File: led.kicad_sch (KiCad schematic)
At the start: 196 parts, among them U1 IS31FL3729, U2 IS31FL3729, U3 IS31FL3729, U4 IS31FL3729

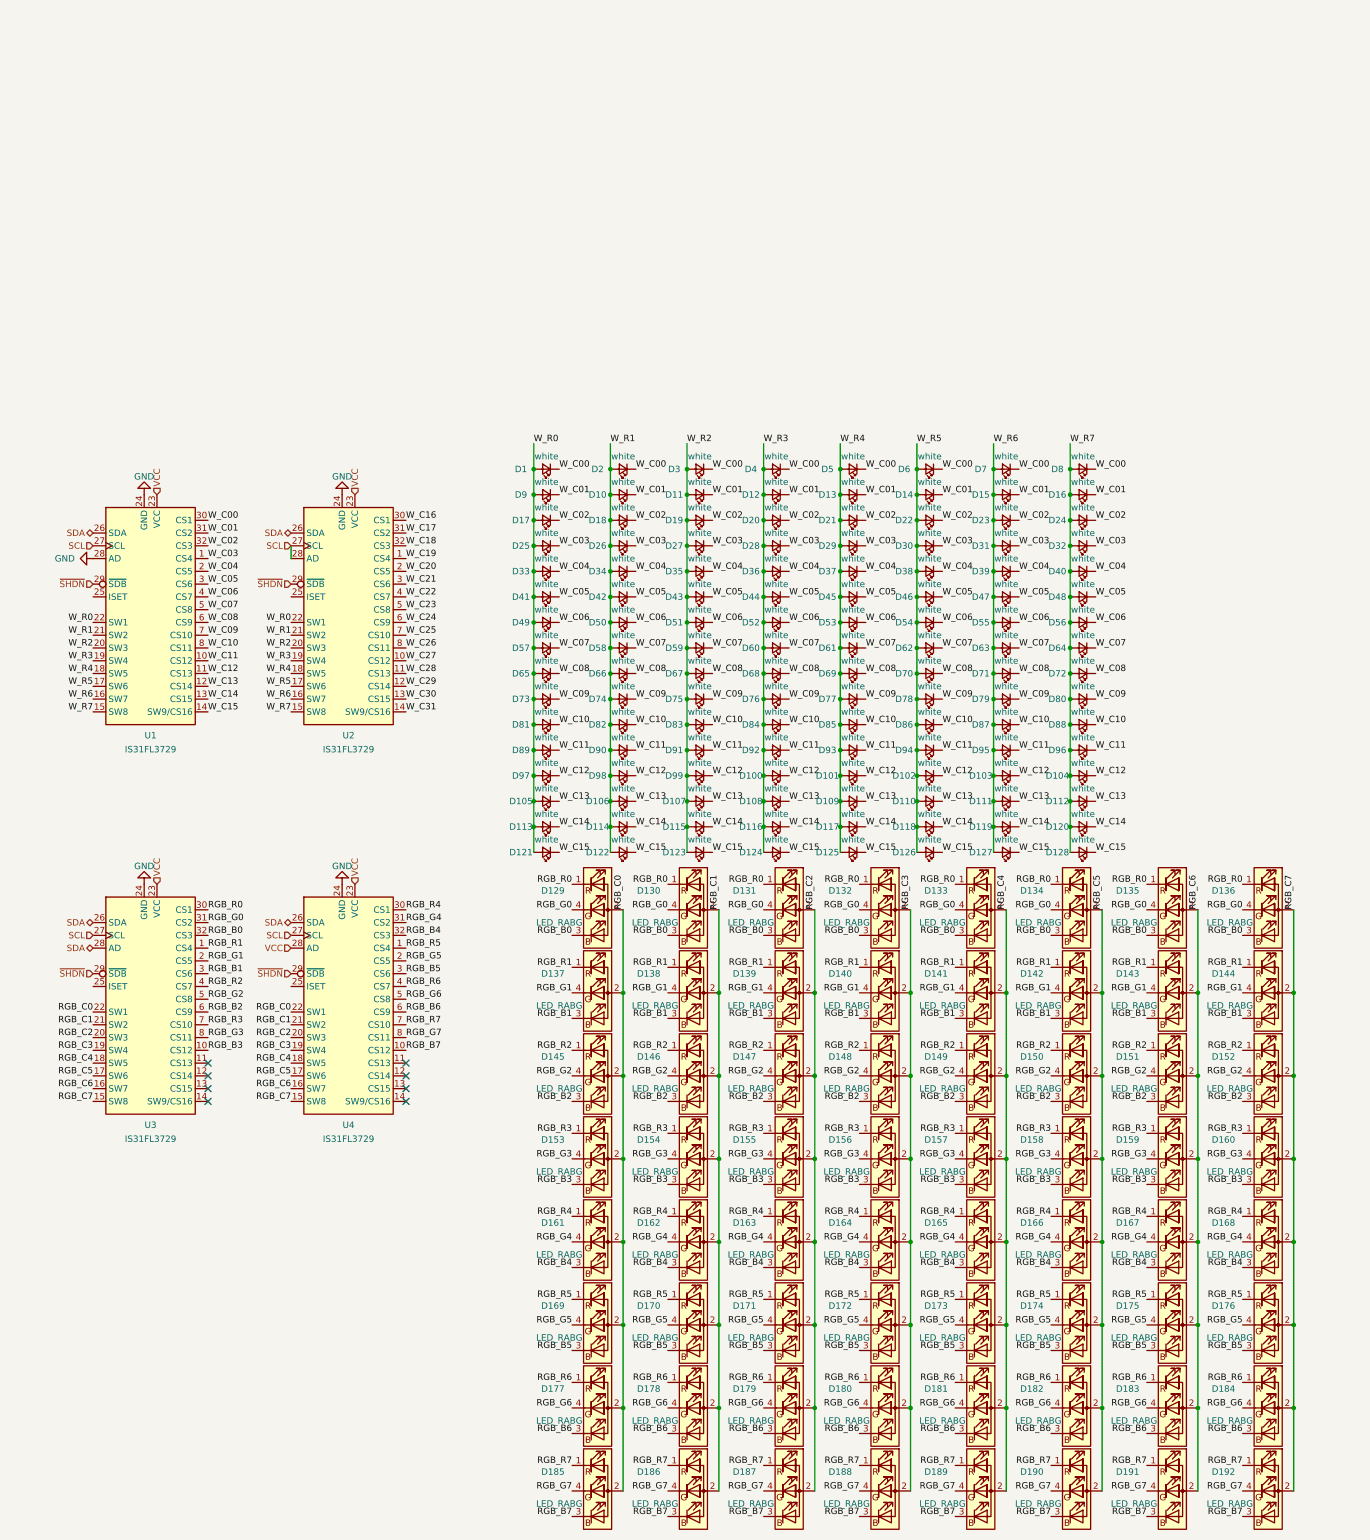
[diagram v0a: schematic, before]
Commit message: routed matrix + PWM driver
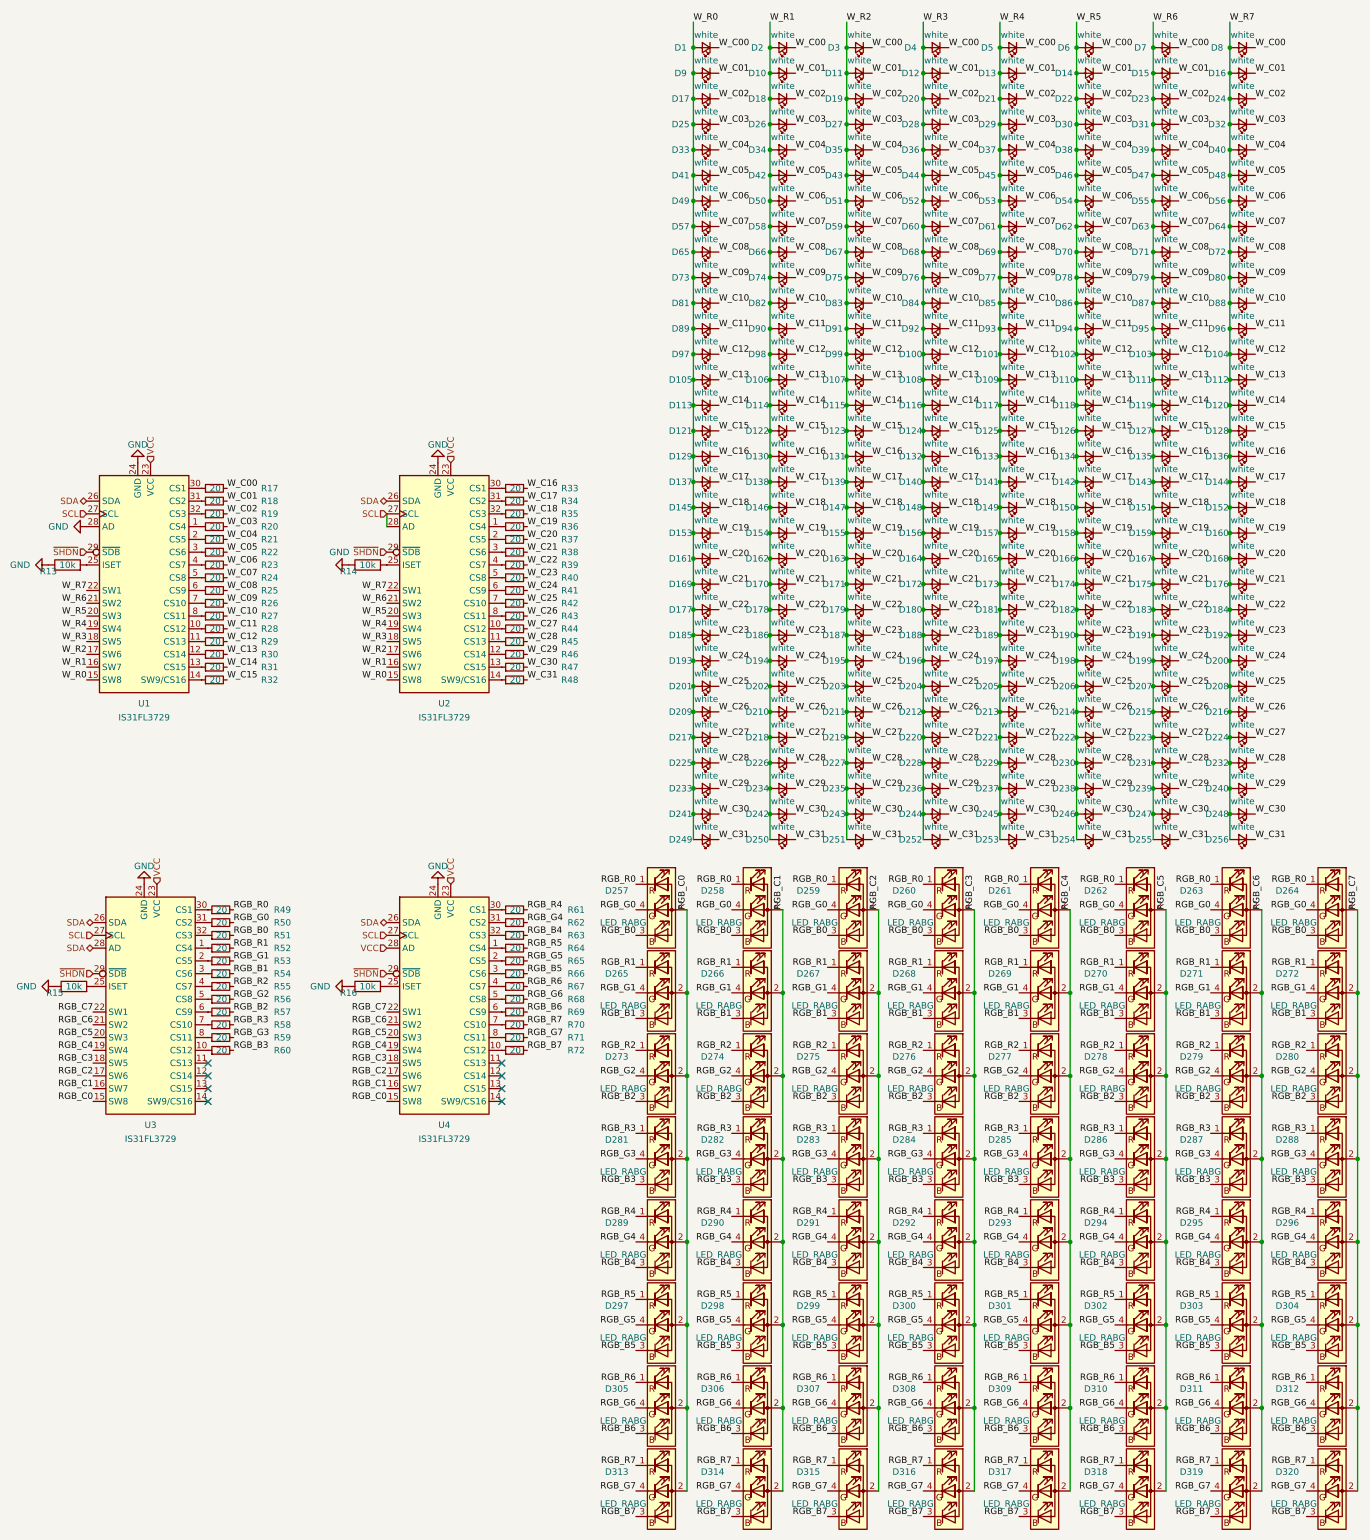
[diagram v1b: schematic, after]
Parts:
- added D129, D130, D131, D132, D133, D134, D135, D136, D137, D138, D139, D140, D141, D142, D143, D144, D145, D146, D147, D148, D149, D150, D151, D152, D153, D154, D155, D156, D157, D158, D159, D160, D161, D162, D163, D164, D165, D166, D167, D168, D169, D170, D171, D172, D173, D174, D175, D176, D177, D178, D179, D180, D181, D182, D183, D184, D185, D186, D187, D188, D189, D190, D191, D192, D193, D194, D195, D196, D197, D198, D199, D200, D201, D202, D203, D204, D205, D206, D207, D208, D209, D210, D211, D212, D213, D214, D215, D216, D217, D218, D219, D220, D221, D222, D223, D224, D225, D226, D227, D228, D229, D230, D231, D232, D233, D234, D235, D236, D237, D238, D239, D240, D241, D242, D243, D244, D245, D246, D247, D248, D249, D250, D251, D252, D253, D254, D255, D256: white, Diode_SMD:D_0603_1608Metric, symbol Device:LED_Small
- added R13, R14, R15, R16: 10k, Resistor_SMD:R_0603_1608Metric, symbol Device:R
- added R17, R18, R19, R20, R21, R22, R23, R24, R25, R26, R27, R28, R29, R30, R31, R32, R33, R34, R35, R36, R37, R38, R39, R40, R41, R42, R43, R44, R45, R46, R47, R48, R49, R50, R51, R52, R53, R54, R55, R56, R57, R58, R59, R60, R61, R62, R63, R64, R65, R66, R67, R68, R69, R70, R71, R72: 20, Resistor_SMD:R_0603_1608Metric, symbol Device:R_Small
- renumbered D129 to D257, D130 to D258, D131 to D259, D132 to D260, D133 to D261, D134 to D262, D135 to D263, D136 to D264, D137 to D265, D138 to D266, D139 to D267, D140 to D268, D141 to D269, D142 to D270, D143 to D271, D144 to D272, D145 to D273, D146 to D274, D147 to D275, D148 to D276, D149 to D277, D150 to D278, D151 to D279, D152 to D280, D153 to D281, D154 to D282, D155 to D283, D156 to D284, D157 to D285, D158 to D286, D159 to D287, D160 to D288, D161 to D289, D162 to D290, D163 to D291, D164 to D292, D165 to D293, D166 to D294, D167 to D295, D168 to D296, D169 to D297, D170 to D298, D171 to D299, D172 to D300, D173 to D301, D174 to D302, D175 to D303, D176 to D304, D177 to D305, D178 to D306, D179 to D307, D180 to D308, D181 to D309, D182 to D310, D183 to D311, D184 to D312, D185 to D313, D186 to D314, D187 to D315, D188 to D316, D189 to D317, D190 to D318, D191 to D319, D192 to D320
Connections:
- net GND: now also R13.1, R14.1, R15.1, R16.1
- net RGB_B0: now also R51.2; no longer U3.32 (CS3)
- net RGB_B1: now also R54.2; no longer U3.3 (CS6)
- net RGB_B2: now also R57.2; no longer U3.6 (CS9)
- net RGB_B3: now also R60.2; no longer U3.10 (CS12)
- net RGB_B4: now also R63.2; no longer U4.32 (CS3)
- net RGB_B5: now also R66.2; no longer U4.3 (CS6)
- net RGB_B6: now also R69.2; no longer U4.6 (CS9)
- net RGB_B7: now also R72.2; no longer U4.10 (CS12)
- net RGB_C0: now also U3.15 (SW8), U4.15 (SW8); no longer U3.22 (SW1), U4.22 (SW1)
- net RGB_C1: now also U3.16 (SW7), U4.16 (SW7); no longer U3.21 (SW2), U4.21 (SW2)
- net RGB_C2: now also U3.17 (SW6), U4.17 (SW6); no longer U3.20 (SW3), U4.20 (SW3)
- net RGB_C3: now also U3.18 (SW5), U4.18 (SW5); no longer U3.19 (SW4), U4.19 (SW4)
- net RGB_C4: now also U3.19 (SW4), U4.19 (SW4); no longer U3.18 (SW5), U4.18 (SW5)
- net RGB_C5: now also U3.20 (SW3), U4.20 (SW3); no longer U3.17 (SW6), U4.17 (SW6)
- net RGB_C6: now also U3.21 (SW2), U4.21 (SW2); no longer U3.16 (SW7), U4.16 (SW7)
- net RGB_C7: now also U3.22 (SW1), U4.22 (SW1); no longer U3.15 (SW8), U4.15 (SW8)
- net RGB_G0: now also R50.2; no longer U3.31 (CS2)
- net RGB_G1: now also R53.2; no longer U3.2 (CS5)
- net RGB_G2: now also R56.2; no longer U3.5 (CS8)
- net RGB_G3: now also R59.2; no longer U3.8 (CS11)
- net RGB_G4: now also R62.2; no longer U4.31 (CS2)
- net RGB_G5: now also R65.2; no longer U4.2 (CS5)
- net RGB_G6: now also R68.2; no longer U4.5 (CS8)
- net RGB_G7: now also R71.2; no longer U4.8 (CS11)
- net RGB_R0: now also R49.2; no longer U3.30 (CS1)
- net RGB_R1: now also R52.2; no longer U3.1 (CS4)
- net RGB_R2: now also R55.2; no longer U3.4 (CS7)
- net RGB_R3: now also R58.2; no longer U3.7 (CS10)
- net RGB_R4: now also R61.2; no longer U4.30 (CS1)
- net RGB_R5: now also R64.2; no longer U4.1 (CS4)
- net RGB_R6: now also R67.2; no longer U4.4 (CS7)
- net RGB_R7: now also R70.2; no longer U4.7 (CS10)
- net W_C00: now also R17.2; no longer U1.30 (CS1)
- net W_C01: now also R18.2; no longer U1.31 (CS2)
- net W_C02: now also R19.2; no longer U1.32 (CS3)
- net W_C03: now also R20.2; no longer U1.1 (CS4)
- net W_C04: now also R21.2; no longer U1.2 (CS5)
- net W_C05: now also R22.2; no longer U1.3 (CS6)
- net W_C06: now also R23.2; no longer U1.4 (CS7)
- net W_C07: now also R24.2; no longer U1.5 (CS8)
- net W_C08: now also R25.2; no longer U1.6 (CS9)
- net W_C09: now also R26.2; no longer U1.7 (CS10)
- net W_C10: now also R27.2; no longer U1.8 (CS11)
- net W_C11: now also R28.2; no longer U1.10 (CS12)
- net W_C12: now also R29.2; no longer U1.11 (CS13)
- net W_C13: now also R30.2; no longer U1.12 (CS14)
- net W_C14: now also R31.2; no longer U1.13 (CS15)
- net W_C15: now also R32.2; no longer U1.14 (SW9/CS16)
- net W_C16: now also D129.1 (K), D130.1 (K), D131.1 (K), D132.1 (K), D133.1 (K), D134.1 (K), D135.1 (K), D136.1 (K), R33.2; no longer U2.30 (CS1)
- net W_C17: now also D137.1 (K), D138.1 (K), D139.1 (K), D140.1 (K), D141.1 (K), D142.1 (K), D143.1 (K), D144.1 (K), R34.2; no longer U2.31 (CS2)
- net W_C18: now also D145.1 (K), D146.1 (K), D147.1 (K), D148.1 (K), D149.1 (K), D150.1 (K), D151.1 (K), D152.1 (K), R35.2; no longer U2.32 (CS3)
- net W_C19: now also D153.1 (K), D154.1 (K), D155.1 (K), D156.1 (K), D157.1 (K), D158.1 (K), D159.1 (K), D160.1 (K), R36.2; no longer U2.1 (CS4)
- net W_C20: now also D161.1 (K), D162.1 (K), D163.1 (K), D164.1 (K), D165.1 (K), D166.1 (K), D167.1 (K), D168.1 (K), R37.2; no longer U2.2 (CS5)
- net W_C21: now also D169.1 (K), D170.1 (K), D171.1 (K), D172.1 (K), D173.1 (K), D174.1 (K), D175.1 (K), D176.1 (K), R38.2; no longer U2.3 (CS6)
- net W_C22: now also D177.1 (K), D178.1 (K), D179.1 (K), D180.1 (K), D181.1 (K), D182.1 (K), D183.1 (K), D184.1 (K), R39.2; no longer U2.4 (CS7)
- net W_C23: now also D185.1 (K), D186.1 (K), D187.1 (K), D188.1 (K), D189.1 (K), D190.1 (K), D191.1 (K), D192.1 (K), R40.2; no longer U2.5 (CS8)
- net W_C24: now also D193.1 (K), D194.1 (K), D195.1 (K), D196.1 (K), D197.1 (K), D198.1 (K), D199.1 (K), D200.1 (K), R41.2; no longer U2.6 (CS9)
- net W_C25: now also D201.1 (K), D202.1 (K), D203.1 (K), D204.1 (K), D205.1 (K), D206.1 (K), D207.1 (K), D208.1 (K), R42.2; no longer U2.7 (CS10)
- net W_C26: now also D209.1 (K), D210.1 (K), D211.1 (K), D212.1 (K), D213.1 (K), D214.1 (K), D215.1 (K), D216.1 (K), R43.2; no longer U2.8 (CS11)
- net W_C27: now also D217.1 (K), D218.1 (K), D219.1 (K), D220.1 (K), D221.1 (K), D222.1 (K), D223.1 (K), D224.1 (K), R44.2; no longer U2.10 (CS12)
- net W_C28: now also D225.1 (K), D226.1 (K), D227.1 (K), D228.1 (K), D229.1 (K), D230.1 (K), D231.1 (K), D232.1 (K), R45.2; no longer U2.11 (CS13)
- net W_C29: now also D233.1 (K), D234.1 (K), D235.1 (K), D236.1 (K), D237.1 (K), D238.1 (K), D239.1 (K), D240.1 (K), R46.2; no longer U2.12 (CS14)
- net W_C30: now also D241.1 (K), D242.1 (K), D243.1 (K), D244.1 (K), D245.1 (K), D246.1 (K), D247.1 (K), D248.1 (K), R47.2; no longer U2.13 (CS15)
- net W_C31: now also D249.1 (K), D250.1 (K), D251.1 (K), D252.1 (K), D253.1 (K), D254.1 (K), D255.1 (K), D256.1 (K), R48.2; no longer U2.14 (SW9/CS16)
- net W_R0: now also U1.15 (SW8), U2.15 (SW8), D129.2 (A), D137.2 (A), D145.2 (A), D153.2 (A), D161.2 (A), D169.2 (A), D177.2 (A), D185.2 (A), D193.2 (A), D201.2 (A), D209.2 (A), D217.2 (A), D225.2 (A), D233.2 (A), D241.2 (A), D249.2 (A); no longer U1.22 (SW1), U2.22 (SW1)
- net W_R1: now also U1.16 (SW7), U2.16 (SW7), D130.2 (A), D138.2 (A), D146.2 (A), D154.2 (A), D162.2 (A), D170.2 (A), D178.2 (A), D186.2 (A), D194.2 (A), D202.2 (A), D210.2 (A), D218.2 (A), D226.2 (A), D234.2 (A), D242.2 (A), D250.2 (A); no longer U1.21 (SW2), U2.21 (SW2)
- net W_R2: now also U1.17 (SW6), U2.17 (SW6), D131.2 (A), D139.2 (A), D147.2 (A), D155.2 (A), D163.2 (A), D171.2 (A), D179.2 (A), D187.2 (A), D195.2 (A), D203.2 (A), D211.2 (A), D219.2 (A), D227.2 (A), D235.2 (A), D243.2 (A), D251.2 (A); no longer U1.20 (SW3), U2.20 (SW3)
- net W_R3: now also U1.18 (SW5), U2.18 (SW5), D132.2 (A), D140.2 (A), D148.2 (A), D156.2 (A), D164.2 (A), D172.2 (A), D180.2 (A), D188.2 (A), D196.2 (A), D204.2 (A), D212.2 (A), D220.2 (A), D228.2 (A), D236.2 (A), D244.2 (A), D252.2 (A); no longer U1.19 (SW4), U2.19 (SW4)
- net W_R4: now also U1.19 (SW4), U2.19 (SW4), D133.2 (A), D141.2 (A), D149.2 (A), D157.2 (A), D165.2 (A), D173.2 (A), D181.2 (A), D189.2 (A), D197.2 (A), D205.2 (A), D213.2 (A), D221.2 (A), D229.2 (A), D237.2 (A), D245.2 (A), D253.2 (A); no longer U1.18 (SW5), U2.18 (SW5)
- net W_R5: now also U1.20 (SW3), U2.20 (SW3), D134.2 (A), D142.2 (A), D150.2 (A), D158.2 (A), D166.2 (A), D174.2 (A), D182.2 (A), D190.2 (A), D198.2 (A), D206.2 (A), D214.2 (A), D222.2 (A), D230.2 (A), D238.2 (A), D246.2 (A), D254.2 (A); no longer U1.17 (SW6), U2.17 (SW6)
- net W_R6: now also U1.21 (SW2), U2.21 (SW2), D135.2 (A), D143.2 (A), D151.2 (A), D159.2 (A), D167.2 (A), D175.2 (A), D183.2 (A), D191.2 (A), D199.2 (A), D207.2 (A), D215.2 (A), D223.2 (A), D231.2 (A), D239.2 (A), D247.2 (A), D255.2 (A); no longer U1.16 (SW7), U2.16 (SW7)
- net W_R7: now also U1.22 (SW1), U2.22 (SW1), D136.2 (A), D144.2 (A), D152.2 (A), D160.2 (A), D168.2 (A), D176.2 (A), D184.2 (A), D192.2 (A), D200.2 (A), D208.2 (A), D216.2 (A), D224.2 (A), D232.2 (A), D240.2 (A), D248.2 (A), D256.2 (A); no longer U1.15 (SW8), U2.15 (SW8)
- net at U1.25 (ISET): now also R13.2
- net at U4.25 (ISET): now also R16.2
- net at U2.25 (ISET): now also R14.2
- net at U3.25 (ISET): now also R15.2
- new net: R20.1, U1.1 (CS4)
- new net: R28.1, U1.10 (CS12)
- new net: R29.1, U1.11 (CS13)
- new net: R30.1, U1.12 (CS14)
- new net: R31.1, U1.13 (CS15)
- new net: R32.1, U1.14 (SW9/CS16)
- new net: R21.1, U1.2 (CS5)
- new net: R22.1, U1.3 (CS6)
- new net: R17.1, U1.30 (CS1)
- new net: R18.1, U1.31 (CS2)
- new net: R19.1, U1.32 (CS3)
- new net: R23.1, U1.4 (CS7)
- new net: R24.1, U1.5 (CS8)
- new net: R25.1, U1.6 (CS9)
- new net: R26.1, U1.7 (CS10)
- new net: R27.1, U1.8 (CS11)
- new net: R47.1, U2.13 (CS15)
- new net: R72.1, U4.10 (CS12)
- new net: R59.1, U3.8 (CS11)
- new net: R42.1, U2.7 (CS10)
- new net: R40.1, U2.5 (CS8)
- new net: R34.1, U2.31 (CS2)
- new net: R39.1, U2.4 (CS7)
- new net: R52.1, U3.1 (CS4)
- new net: R38.1, U2.3 (CS6)
- new net: R60.1, U3.10 (CS12)
- new net: R36.1, U2.1 (CS4)
- new net: R67.1, U4.4 (CS7)
- new net: R64.1, U4.1 (CS4)
- new net: R65.1, U4.2 (CS5)
- new net: R66.1, U4.3 (CS6)
- new net: R61.1, U4.30 (CS1)
- new net: R62.1, U4.31 (CS2)
- new net: R63.1, U4.32 (CS3)
- new net: R68.1, U4.5 (CS8)
- new net: R69.1, U4.6 (CS9)
- new net: R70.1, U4.7 (CS10)
- new net: R71.1, U4.8 (CS11)
- new net: R33.1, U2.30 (CS1)
- new net: R44.1, U2.10 (CS12)
- new net: R45.1, U2.11 (CS13)
- new net: R46.1, U2.12 (CS14)
- new net: R48.1, U2.14 (SW9/CS16)
- new net: R37.1, U2.2 (CS5)
- new net: R35.1, U2.32 (CS3)
- new net: R41.1, U2.6 (CS9)
- new net: R43.1, U2.8 (CS11)
- new net: R54.1, U3.3 (CS6)
- new net: R49.1, U3.30 (CS1)
- new net: R58.1, U3.7 (CS10)
- new net: R51.1, U3.32 (CS3)
- new net: R50.1, U3.31 (CS2)
- new net: R55.1, U3.4 (CS7)
- new net: R57.1, U3.6 (CS9)
- new net: R56.1, U3.5 (CS8)
- new net: R53.1, U3.2 (CS5)
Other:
- moved on the sheet: D1, D10, D100, D101, D102, D103, D104, D105, D106, D107, D108, D109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

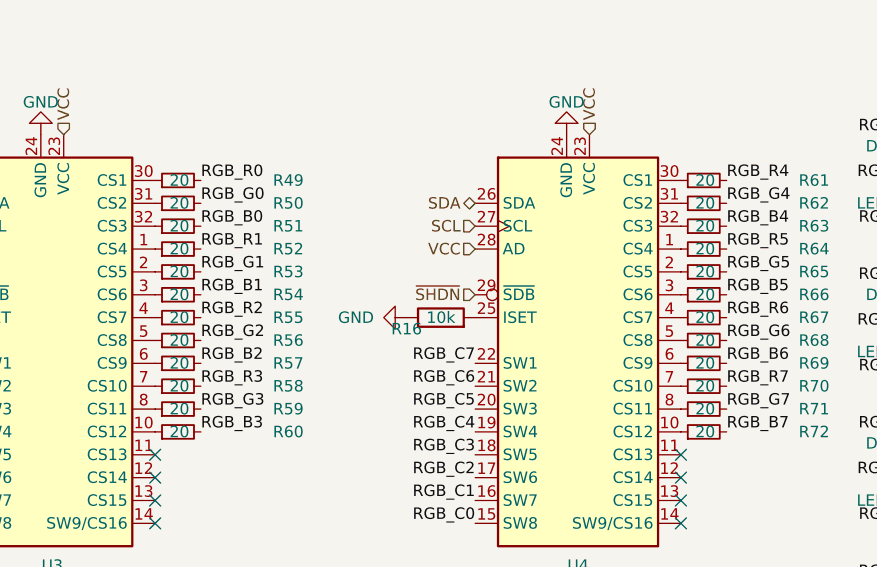
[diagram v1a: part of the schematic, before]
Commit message: routed PMU
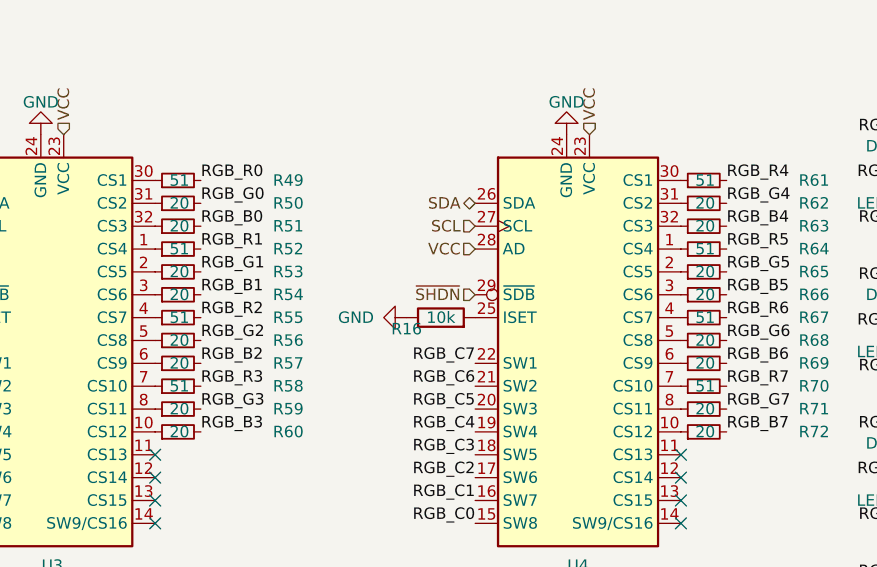
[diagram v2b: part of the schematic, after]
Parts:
- R49, R52, R55, R58, R61, R64, R67, R70: value 20 -> 51
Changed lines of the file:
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@@
       (effects (font (size 1.27 1.27)) (justify left))
     )
-    (property "Value" "20" (id 1) (at 57.15 115.57 90)
+    (property "Value" "51" (id 1) (at 57.15 115.57 90)
       (effects (font (size 1.27 1.27)) (justify left))
     )
@@
       (effects (font (size 1.27 1.27)) (justify left))
     )
-    (property "Value" "20" (id 1) (at 115.57 123.19 90)
+    (property "Value" "51" (id 1) (at 115.57 123.19 90)
       (effects (font (size 1.27 1.27)) (justify left))
     )
@@
       (effects (font (size 1.27 1.27)) (justify left))
     )
-    (property "Value" "20" (id 1) (at 115.57 130.81 90)
+    (property "Value" "51" (id 1) (at 115.57 130.81 90)
       (effects (font (size 1.27 1.27)) (justify left))
     )
@@
       (effects (font (size 1.27 1.27)) (justify left))
     )
-    (property "Value" "20" (id 1) (at 115.57 115.57 90)
+    (property "Value" "51" (id 1) (at 115.57 115.57 90)
       (effects (font (size 1.27 1.27)) (justify left))
     )
@@
       (effects (font (size 1.27 1.27)) (justify left))
     )
-    (property "Value" "20" (id 1) (at 57.15 107.95 90)
+    (property "Value" "51" (id 1) (at 57.15 107.95 90)
       (effects (font (size 1.27 1.27)) (justify left))
     )
@@
       (effects (font (size 1.27 1.27)) (justify left))
     )
-    (property "Value" "20" (id 1) (at 57.15 130.81 90)
+    (property "Value" "51" (id 1) (at 57.15 130.81 90)
       (effects (font (size 1.27 1.27)) (justify left))
     )
@@
       (effects (font (size 1.27 1.27)) (justify left))
     )
-    (property "Value" "20" (id 1) (at 57.15 123.19 90)
+    (property "Value" "51" (id 1) (at 57.15 123.19 90)
       (effects (font (size 1.27 1.27)) (justify left))
     )
@@
       (effects (font (size 1.27 1.27)) (justify left))
     )
-    (property "Value" "20" (id 1) (at 115.57 107.95 90)
+    (property "Value" "51" (id 1) (at 115.57 107.95 90)
       (effects (font (size 1.27 1.27)) (justify left))
     )
